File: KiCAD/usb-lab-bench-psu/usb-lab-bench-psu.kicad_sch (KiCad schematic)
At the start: 5 parts, among them J1 Conn_02x02_Top_Bottom, SW1 SW_Push

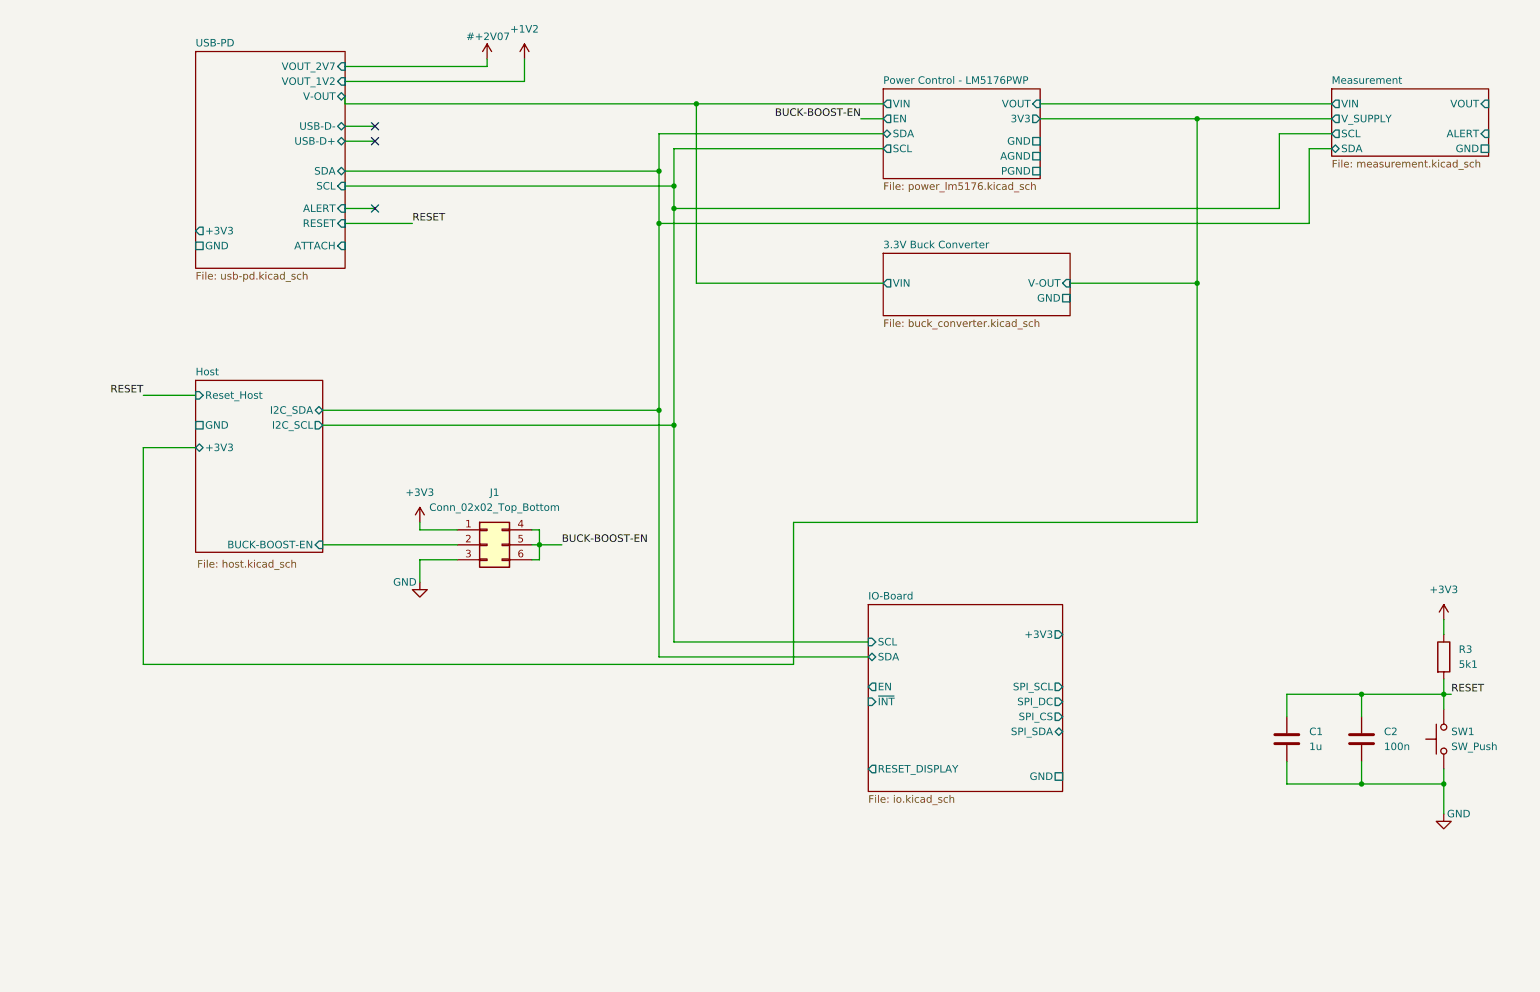
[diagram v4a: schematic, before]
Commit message: restructured schematics to better show individual boards
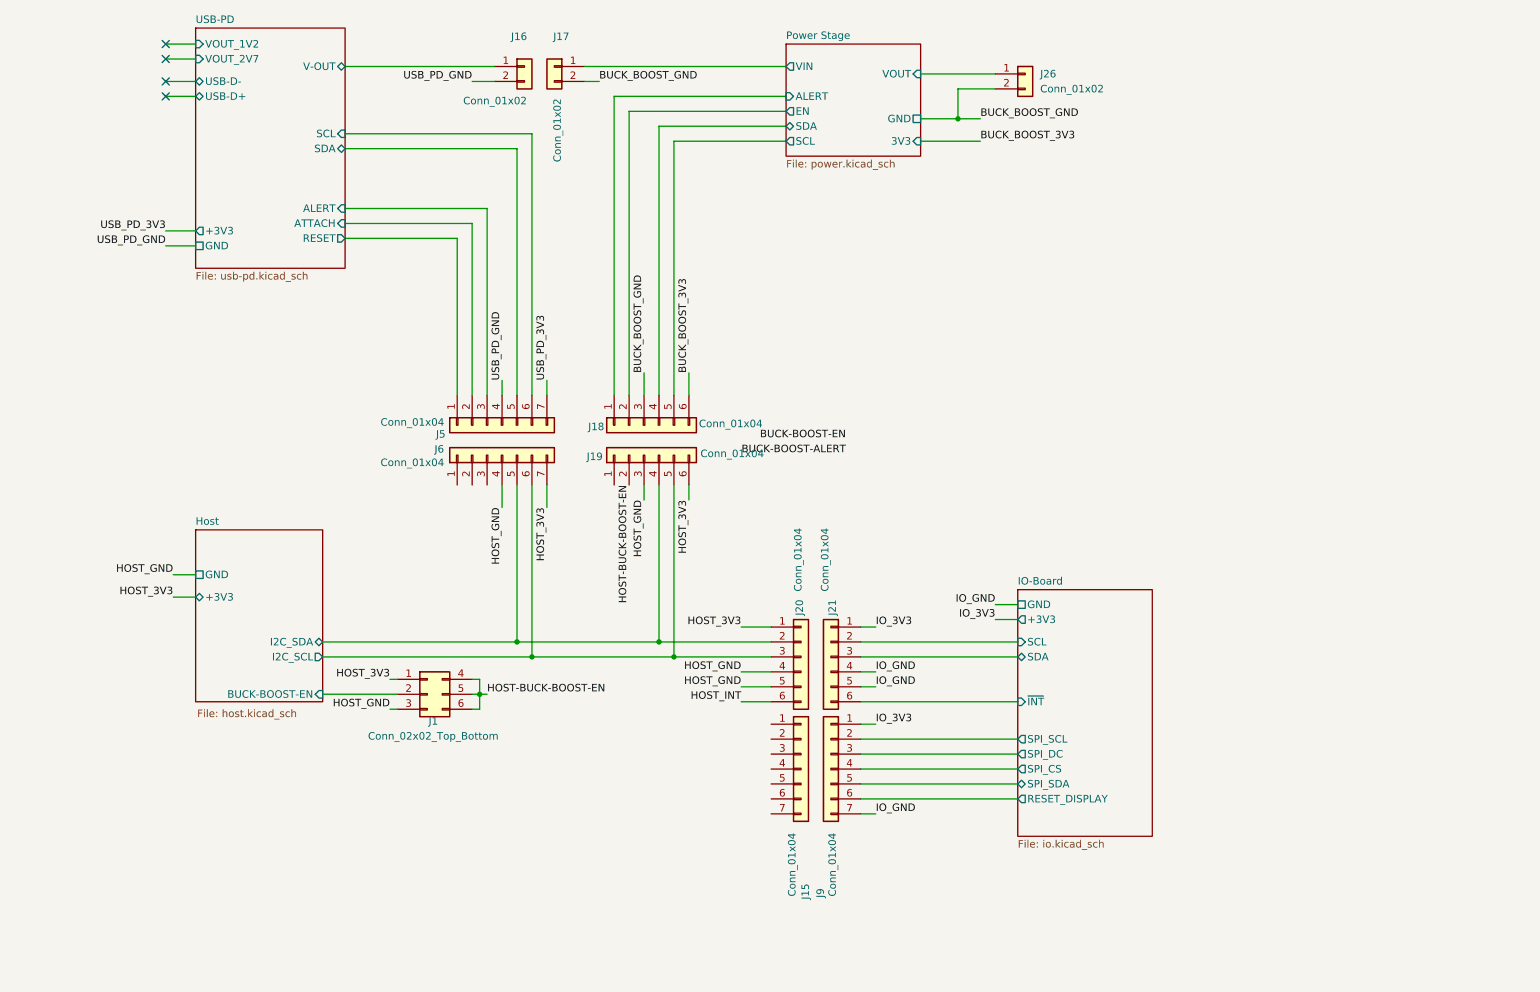
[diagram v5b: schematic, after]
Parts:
- removed C1: 1u, Capacitor_SMD:C_0402_1005Metric_Pad0.74x0.62mm_HandSolder, symbol Device:C
- removed C2: 100n, Capacitor_SMD:C_0402_1005Metric_Pad0.74x0.62mm_HandSolder, symbol Device:C
- removed R3: 5k1, Resistor_SMD:R_0402_1005Metric_Pad0.72x0.64mm_HandSolder, symbol Device:R
- removed SW1: SW_Push, Button_Switch_SMD:SW_SPST_TL3342, symbol Switch:SW_Push
- added J15, J5, J6, J9: Conn_01x04, symbol Connector_Generic:Conn_01x07
- added J16, J17, J26: Conn_01x02, symbol Connector_Generic:Conn_01x02
- added J18, J19, J20, J21: Conn_01x04, symbol Connector_Generic:Conn_01x06
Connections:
- net BUCK-BOOST-EN: no longer J1.4 (Pin_4), J1.5 (Pin_5), J1.6 (Pin_6)
- net Host/I2C_SCL: now also J19.5 (Pin_5), J20.3 (Pin_3), J6.6 (Pin_6)
- net Host/I2C_SDA: now also J19.4 (Pin_4), J20.2 (Pin_2), J6.5 (Pin_5)
- net IO-Board/RESET_DISPLAY: now also J9.6 (Pin_6)
- net IO-Board/SPI_CS: now also J9.4 (Pin_4)
- net IO-Board/SPI_DC: now also J9.3 (Pin_3)
- net IO-Board/SPI_SCL: now also J9.2 (Pin_2)
- net IO-Board/SPI_SDA: now also J9.5 (Pin_5)
- net IO-Board/~{INT}: now also J21.6 (Pin_6)
- net USB-PD/ALERT: now also J5.3 (Pin_3)
- net USB-PD/ATTACH: now also J5.2 (Pin_2)
- net +3V3 renamed HOST_3V3
- net HOST_3V3: now also J19.6 (Pin_6), J20.1 (Pin_1), J6.7 (Pin_7)
- net GND renamed HOST_GND
- net HOST_GND: now also J19.3 (Pin_3), J20.4 (Pin_4), J20.5 (Pin_5), J6.4 (Pin_4)
- new net BUCK_BOOST_3V3: J18.6 (Pin_6)
- new net BUCK_BOOST_GND: J17.2 (Pin_2), J18.3 (Pin_3), J26.2 (Pin_2)
- new net HOST-BUCK-BOOST-EN: J1.4 (Pin_4), J1.5 (Pin_5), J1.6 (Pin_6), J19.2 (Pin_2)
- new net HOST_INT: J20.6 (Pin_6)
- new net IO-Board/SCL: J21.2 (Pin_2)
- new net IO-Board/SDA: J21.3 (Pin_3)
- new net IO_3V3: J21.1 (Pin_1), J9.1 (Pin_1)
- new net IO_GND: J21.4 (Pin_4), J21.5 (Pin_5), J9.7 (Pin_7)
- new net Power Stage/ALERT: J18.1 (Pin_1)
- new net Power Stage/EN: J18.2 (Pin_2)
- new net Power Stage/SCL: J18.5 (Pin_5)
- new net Power Stage/SDA: J18.4 (Pin_4)
- new net Power Stage/VIN: J17.1 (Pin_1)
- new net Power Stage/VOUT: J26.1 (Pin_1)
- new net USB-PD/RESET: J5.1 (Pin_1)
- new net USB-PD/SCL: J5.6 (Pin_6)
- new net USB-PD/SDA: J5.5 (Pin_5)
- new net USB-PD/V-OUT: J16.1 (Pin_1)
- new net USB_PD_3V3: J5.7 (Pin_7)
- new net USB_PD_GND: J16.2 (Pin_2), J5.4 (Pin_4)
- no-connect marks 3 -> 4
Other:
- removed sheet 3.3V Buck Converter
- removed sheet Measurement
- removed sheet Power Control - LM5176PWP
- added sheet Power Stage (power.kicad_sch)
- sheet Host ports: added none; removed Reset_Host
- sheet IO-Board ports: added none; removed EN
- moved on the sheet: J1

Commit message: updated spi for display
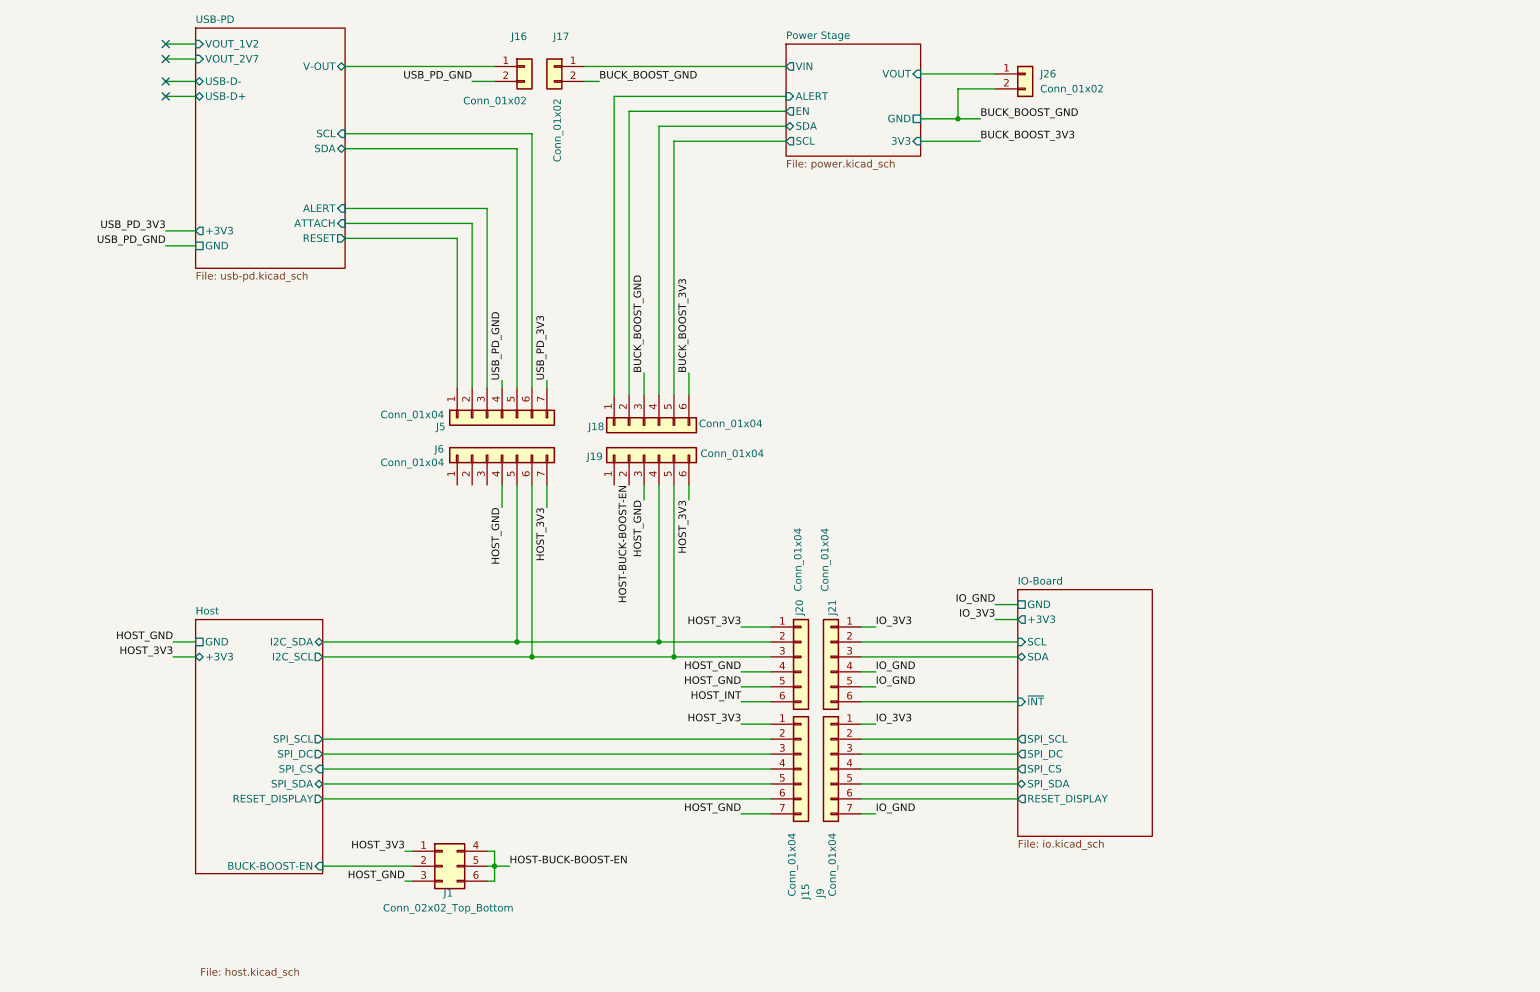
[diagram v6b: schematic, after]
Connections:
- net HOST_3V3: now also J15.1 (Pin_1)
- net HOST_GND: now also J15.7 (Pin_7)
- net Host/SPI_SCL: now reaches J15.2 (Pin_2)
- net Host/SPI_DC: now reaches J15.3 (Pin_3)
- net Host/SPI_CS: now reaches J15.4 (Pin_4)
- net Host/SPI_SDA: now reaches J15.5 (Pin_5)
- net Host/RESET_DISPLAY: now reaches J15.6 (Pin_6)
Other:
- sheet Host ports: added RESET_DISPLAY, SPI_CS, SPI_DC, SPI_SCL, SPI_SDA; removed none
- moved on the sheet: J1, J5

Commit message: added current limiting circuit for USB PD sink, added 2nd buck converter
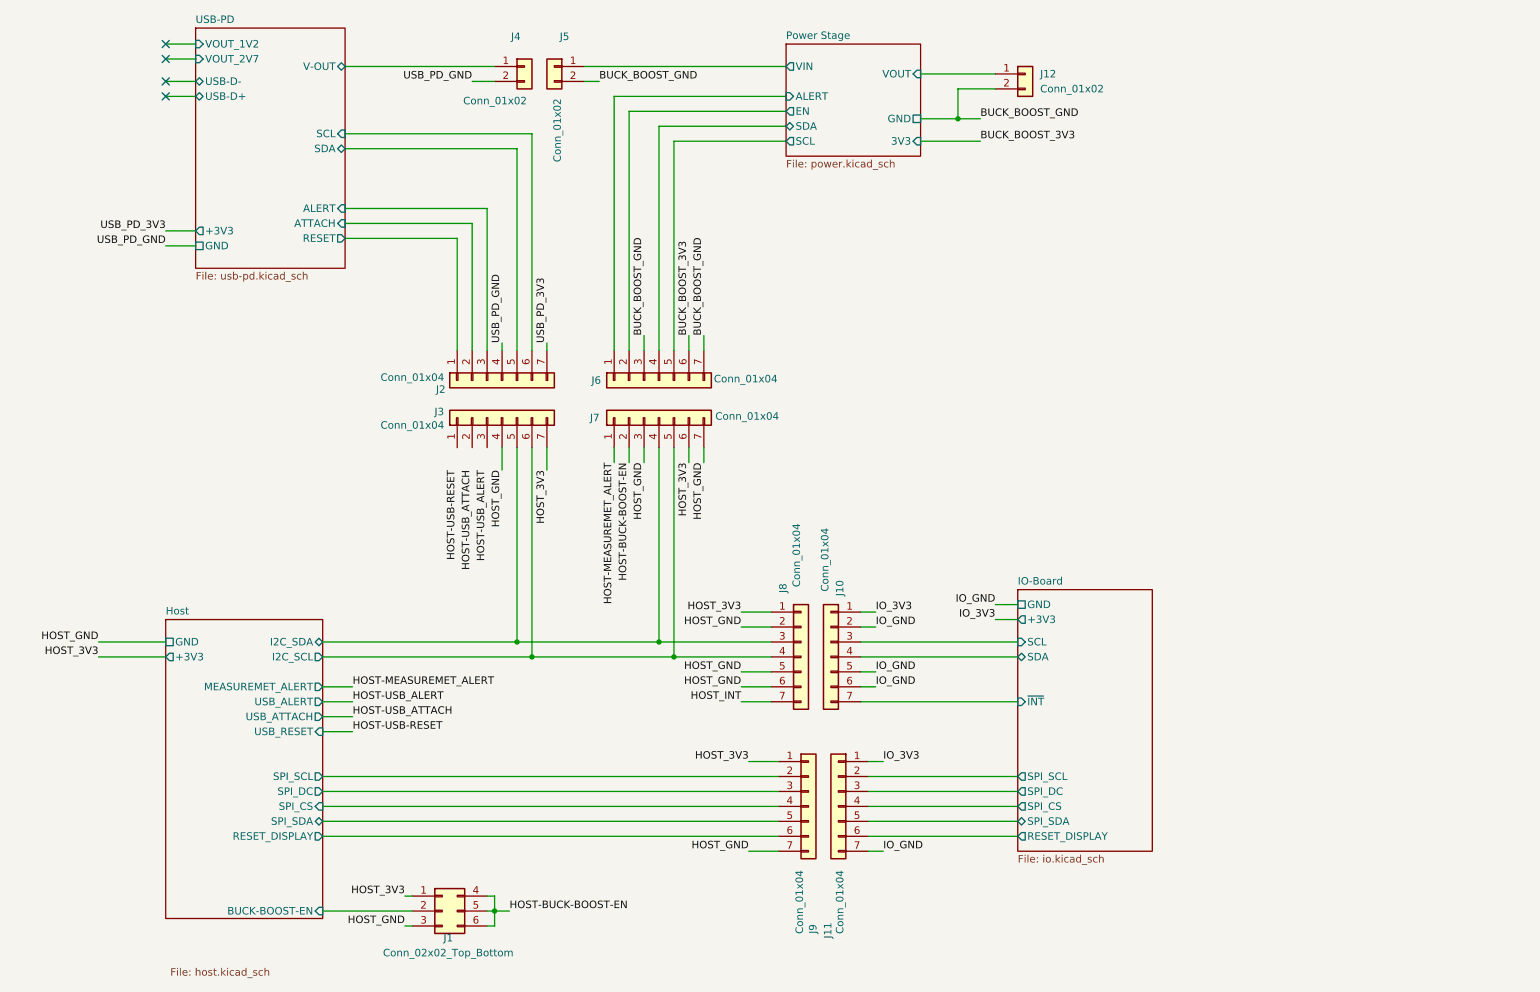
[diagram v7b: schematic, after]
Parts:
- J10: renamed from J21; symbol Connector_Generic:Conn_01x06 -> Connector_Generic:Conn_01x07
- J6: renamed from J18; symbol Connector_Generic:Conn_01x06 -> Connector_Generic:Conn_01x07
- J7: renamed from J19; symbol Connector_Generic:Conn_01x06 -> Connector_Generic:Conn_01x07
- J8: renamed from J20; symbol Connector_Generic:Conn_01x06 -> Connector_Generic:Conn_01x07
- renumbered J9 to J11, J26 to J12, J5 to J2, J6 to J3, J16 to J4, J17 to J5, J15 to J9
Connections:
- net BUCK_BOOST_GND: now also J6.7 (Pin_7)
- net HOST_GND: now also J7.7 (Pin_7), J8.2 (Pin_2), J8.6 (Pin_6); no longer J8.4 (Pin_4)
- net HOST_INT: now also J8.7 (Pin_7); no longer J8.6 (Pin_6)
- net Host/I2C_SCL: now also J8.4 (Pin_4); no longer J8.3 (Pin_3)
- net Host/I2C_SDA: now also J8.3 (Pin_3); no longer J8.2 (Pin_2)
- net IO-Board/SCL: now also J10.3 (Pin_3); no longer J10.2 (Pin_2)
- net IO-Board/SDA: now also J10.4 (Pin_4); no longer J10.3 (Pin_3)
- net IO-Board/~{INT}: now also J10.7 (Pin_7); no longer J10.6 (Pin_6)
- net IO_GND: now also J10.2 (Pin_2), J10.6 (Pin_6); no longer J10.4 (Pin_4)
- net HOST-MEASUREMET_ALERT: now reaches J7.1 (Pin_1)
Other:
- sheet Host ports: added MEASUREMET_ALERT, USB_ALERT, USB_ATTACH, USB_RESET; removed none
- moved on the sheet: J1, J11, J2, J3, J9
